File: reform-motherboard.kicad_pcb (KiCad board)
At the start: 4 copper layers, 130 x 99 mm, 208 parts, among them J1 TinyRex-J1-DF40C, J10 TEST_PMIC_ON, J11 TEST_ON, J12 USB_INT_3, J13 Conn_HDMI, J14 Conn_LVDS, J15 USB_INT_2, J16 Conn_LineIn, J17 Conn_LineOut, J18 TRRS, J19 Conn_BOOT, J2 TinyRex-J2-DF40C, J20 Conn_GPIO1, J21 Conn_01x06, J22 Conn_PWRON, J23 Conn_RESET, J24 Conn_01x04, J25 Conn_CONSOLE, J26 Conn_Backlight, J27 48099-5701, J3 TinyRex-J3-DF40C, J4 693072010801, J5 USB_A, J6 Barrel_Jack, J7 USB_A, J8 TEST_3V, J9 USB_INT_1, P1 5622-4100-ML, P2 J0G-0003NL, Q1 2N7002, Q3 2N7002, Q4 Si5481DU, SW1 SW_DIP_x01, U1 MPCIE-Socket, U10 SGTL5000XNAA3, U11 LP3962EMP-2.5, U12 SN74LVC1G08DCKR, U13 TLV1117-15, U14 CM2020-00TR, U15 TPS2044BDR, U16 TUSB2046BVFR, U2 LTC4156IUFDPBF, U3 TPS61235RWLR, U4 AP1501A-33K5G-13, U5 74AHC1G14, U6 INA260AIPW, U7 LTC4415IMSEPBF, U8 INA260AIPW, Y1 6MHz

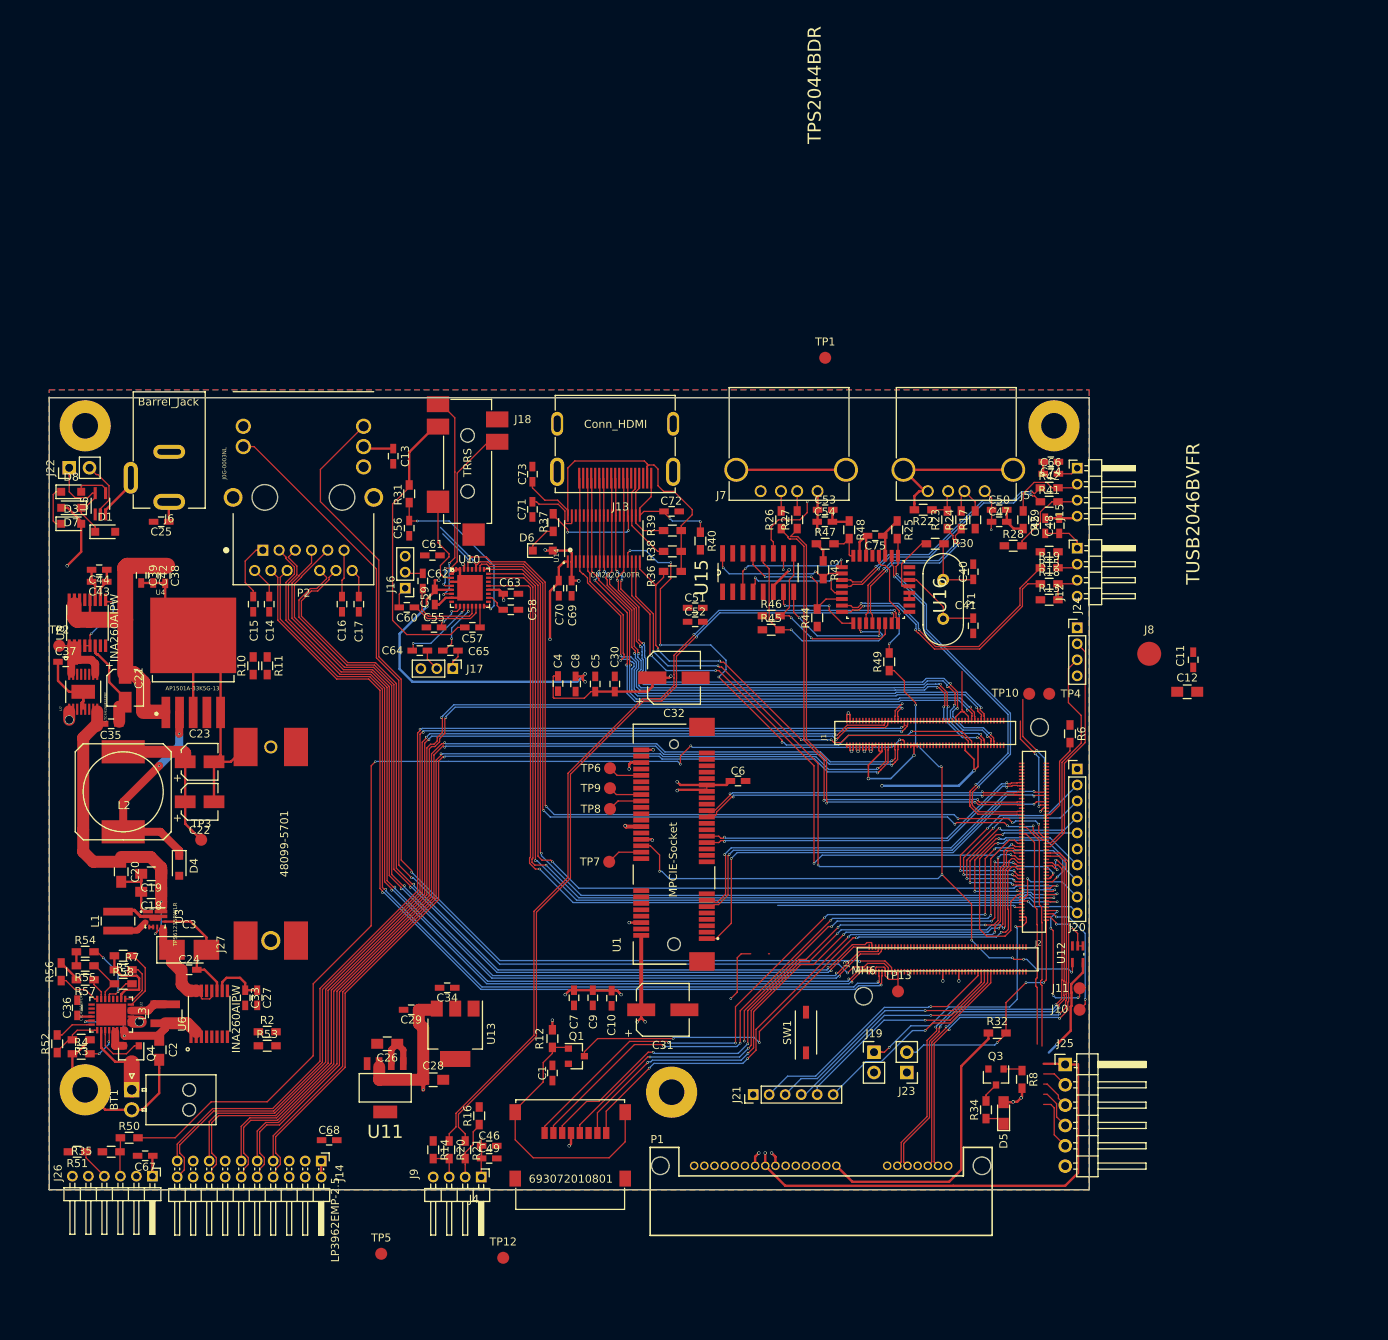
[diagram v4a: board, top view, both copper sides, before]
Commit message: Reform 0.2 main PCB routing WIP, 119 nets to go
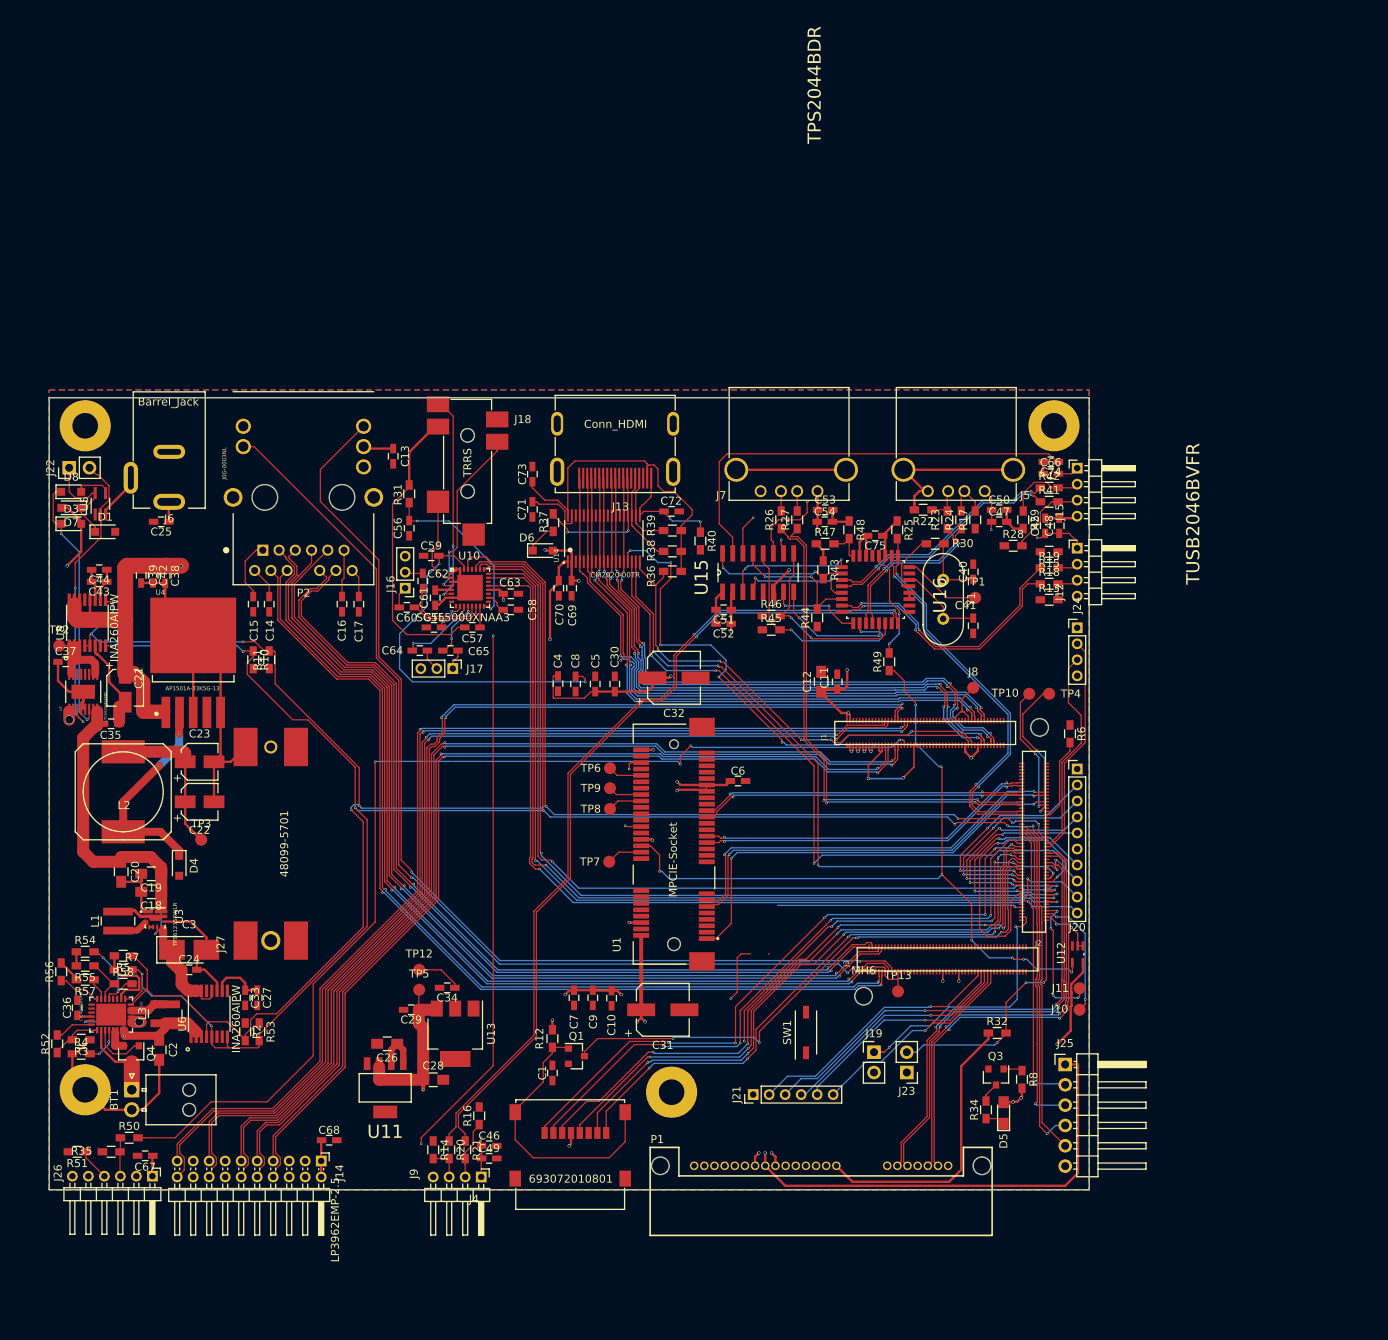
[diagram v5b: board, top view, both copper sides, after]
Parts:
- J8: footprint Measurement_Points:Measurement_Point_Round-SMD-Pad_Big -> Measurement_Points:Measurement_Point_Round-SMD-Pad_Small
- moved C12 45.8 mm to (126.5, 56.5), turned to 90 degrees
- moved C11 44.6 mm to (128.5, 56.5)
- moved TP12 37.5 mm to (76.2, 92.5)
- moved TP1 35.4 mm to (145.8, 46.0)
- moved TP5 33.3 mm to (76.2, 95.0)
- moved J8 22.4 mm to (145.5, 57.2)
- moved C61 5.31 mm to (78.2, 46.0), turned to 90 degrees
- moved C59 5.17 mm to (77.8, 40.8), turned to 0 degrees
- moved C51 3.56 mm to (114.3, 47.5), turned to 180 degrees
- moved C52 3.56 mm to (114.3, 49.2), turned to 180 degrees
- moved R2 2.75 mm to (54.5, 100.2), turned to 270 degrees
- moved R53 2.02 mm to (56.2, 100.2), turned to 270 degrees
- moved R11 0.79 mm to (57.5, 53.8), turned to 90 degrees
- moved R10 0.75 mm to (55.5, 53.8), turned to 270 degrees
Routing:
- net I2C3_SCL: track 125.9 -> 248.6 mm, vias 7 -> 9
- net I2C3_SDA: track 116.8 -> 237.1 mm, vias 5 -> 9
- net +5V: track 159.7 -> 278.7 mm, vias 13 -> 16
- net USB_HUB0_5V: track 4.14 -> 59.5 mm
- net USB_HUB1_5V: track 5.25 -> 48.0 mm, vias 0 -> 2
- net UART1_RTS: track 5.28 -> 42.4 mm, vias 0 -> 1
- net UART1_TXD: track 3.26 -> 35.8 mm, vias 0 -> 1
- net PWRON: track 7.40 -> 37.0 mm, vias 0 -> 2
- net POK_1V5: track 56.0 -> 85.3 mm, vias 10 -> 7
- net BATOFF: track 5.59 -> 32.9 mm, vias 0 -> 2
- net USB_HUB3_5V: track 104.4 -> 125.3 mm, vias 2 -> 4
- net Net-(TP1-Pad1): track 0.00 -> 9.81 mm
- net UART1_RXD: track 31.6 -> 38.9 mm, vias 0 -> 1
- net UART1_CTS: track 35.7 -> 42.5 mm
- net GND: track 196.8 -> 201.1 mm
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- removed copper zone on Power.Cu, net +1V5

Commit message: reform 0.2 main pcb done / rc1
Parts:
- removed Q3: 2N7002, TO_SOT_Packages_SMD:SOT-23
- removed SW1: SW_DIP_x01, Buttons_Switches_SMD:SW_DIP_x1_W5.08mm_Slide_Copal_CHS-A
- added G***: LOGO, mnt:mnt, F.Cu at (65.8, 56.6)
- added G***: LOGO, mnt:reform02, F.Cu at (80.1, 58.7)
- added J28: Conn_SDWP, Pin_Headers:Pin_Header_Straight_1x02_Pitch2.54mm, F.Cu at (124.0, 101.5)
- added J29: Conn_5V, Pin_Headers:Pin_Header_Angled_1x02_Pitch2.54mm, F.Cu at (153.2, 117.0)
- J22: footprint Pin_Headers:Pin_Header_Straight_1x02_Pitch2.54mm -> Pin_Headers:Pin_Header_Straight_1x02_Pitch2.00mm
- J24: footprint Pin_Headers:Pin_Header_Straight_1x04_Pitch2.00mm -> Pin_Headers:Pin_Header_Angled_1x04_Pitch2.00mm
- U2: footprint LTC4156IUFDPBF:QFN-28_UFD -> LTC4156-Custom:QFN-28_UFD
- moved R8 64.2 mm to (88.0, 97.8)
- moved BT1 32.4 mm to (72.5, 111.0), turned to 180 degrees
- moved C26 5.52 mm to (71.8, 96.2)
- moved U11 5.52 mm to (71.5, 101.8)
- moved D5 4.04 mm to (146.2, 107.8)
- moved TP5 2.92 mm to (74.8, 92.5)
- moved R34 1.55 mm to (147.5, 111.5), turned to 0 degrees
- moved C29 1.41 mm to (76.2, 96.5), turned to 90 degrees
- moved TP12 1.00 mm to (77.2, 92.5)
- moved J18 0.46 mm to (82.2, 29.6)
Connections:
- C37 pad 1: POK_5V -> Net-(C37-Pad1)
- J2 pad 34: GND -> Net-(J2-Pad34)
- J2 pad 7: POK_5V -> +5V
- R34 pad 2: Net-(Q3-Pad3) -> GND
- TP2 pad 1: POK_5V -> Net-(C37-Pad1)
- U7 pad 10: POK_5V -> Net-(C37-Pad1)
- U7 pad 15: POK_5V -> Net-(C37-Pad1)
- U7 pad 16: POK_5V -> Net-(C37-Pad1)
- U7 pad 9: POK_5V -> Net-(C37-Pad1)
- U8 pad 1: POK_5V -> Net-(C37-Pad1)
- U8 pad 2: POK_5V -> Net-(C37-Pad1)
- U8 pad 3: POK_5V -> Net-(C37-Pad1)
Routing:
- net GND: track 201.1 -> 352.6 mm, vias 0 -> 83
- net +5V: track 278.7 -> 426.5 mm, vias 16 -> 15
- net +3V3: track 192.0 -> 241.3 mm, vias 17 -> 33
- net POK_3V3: track 33.1 -> 75.4 mm, vias 1 -> 2
- net POK_1V5: track 85.3 -> 122.0 mm
- net Net-(BT1-Pad1): track 10.2 -> 43.5 mm, vias 0 -> 1
- net Net-(C18-Pad1): track 39.7 -> 68.0 mm, vias 2 -> 6
- net Net-(C37-Pad1): track 0.00 -> 16.5 mm
- net POK_5V: track 11.1 -> 0.00 mm
- net Net-(C24-Pad1): track 19.2 -> 29.0 mm
- net Net-(C25-Pad1): track 99.0 -> 105.9 mm, vias 3 -> 4
- net SD3_WP: track 50.5 -> 55.8 mm
- net POK_2V5: track 103.6 -> 107.9 mm
- net I2C3_SCL: track 248.6 -> 252.7 mm
- net Net-(Q3-Pad3): track 2.52 -> 0.00 mm
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- added copper zone on Power.Cu, net +3V3

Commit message: reform 0.2 main pcb sent to manufacture
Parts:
- moved TP12 0.79 mm to (77.0, 93.2)
- moved TP5 0.75 mm to (74.8, 93.2)

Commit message: motherboard 0.3 WIP snapshot schematics/PCB
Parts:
- removed BT1: Molex 105313-1202, Connectors_Molex:Molex_NanoFit_1x02x2.50mm_Angled
- removed G***: LOGO, mnt:mnt
- removed G***: LOGO, mnt:reform02
- removed P1: 5622-4100-ML, 5622-4100-ML:3M_5622-4100-ML
- removed Q4: Si5481DU, TO_SOT_Packages_SMD:SOT-23
- removed R41, R42: 27, Resistors_SMD:R_0603_HandSoldering
- removed R47, R48, R56, R58: 0, Resistors_SMD:R_0603_HandSoldering
- removed R50, R51: R0, Resistors_SMD:R_0603_HandSoldering
- removed R52: 100k, Resistors_SMD:R_0603_HandSoldering
- removed R53: 4.7k, Resistors_SMD:R_0603_HandSoldering
- removed R54, R55: 1.21k, Resistors_SMD:R_0603_HandSoldering
- removed R57: 3.6k, Resistors_SMD:R_0603_HandSoldering
- removed U16: TUSB2046BVFR, TUSB2046BVFR:QFP80P900X900X145-32N
- added C76: 10uF, Capacitors_SMD:C_0603_HandSoldering, F.Cu at (99.5, 104.0)
- added C77: 0.1uF, Capacitors_SMD:C_0603_HandSoldering, F.Cu at (99.5, 102.5)
- added C78: 33pF, Capacitors_SMD:C_0603_HandSoldering, F.Cu at (94.0, 102.5)
- added C79: 33pF, Capacitors_SMD:C_0603_HandSoldering, F.Cu at (96.0, 102.5)
- added C80: 33pF, Capacitors_SMD:C_0603_HandSoldering, F.Cu at (92.0, 102.5)
- added C81: 0.1uF, Capacitors_SMD:C_0603_HandSoldering, F.Cu at (104.0, 111.0)
- added C82: 10uF, Capacitors_SMD:C_0603_HandSoldering, F.Cu at (102.5, 99.0)
- added C83: 0.1uF, Capacitors_SMD:C_0603_HandSoldering, F.Cu at (137.5, 38.5)
- added C84: 0.1uF, Capacitors_SMD:C_0603_HandSoldering, F.Cu at (134.5, 57.0)
- added C85: 10uF, Capacitors_SMD:C_0603_HandSoldering, F.Cu at (137.5, 57.0)
- added C86: 0.1uF, Capacitors_SMD:C_0603_HandSoldering, F.Cu at (132.5, 38.5)
- added C87: 0.1uF, Capacitors_SMD:C_0603_HandSoldering, F.Cu at (143.5, 41.5)
- added C88: 0.1uF, Capacitors_SMD:C_0603_HandSoldering, F.Cu at (79.0, 116.0)
- added C89: 10uF, Capacitors_SMD:C_0603_HandSoldering, F.Cu at (75.0, 116.0)
- added C90: 0.1uF, Capacitors_SMD:C_0603_HandSoldering, F.Cu at (71.1, 116.0)
- added C91: 0.1uF, Capacitors_SMD:C_0603_HandSoldering, F.Cu at (75.0, 114.0)
- added D10: LED_WWAN, LEDs:LED_0805_HandSoldering, F.Cu at (103.5, 116.5)
- added D11: LED_3V3, LEDs:LED_0805_HandSoldering, F.Cu at (51.0, 24.2)
- added D2: PDS1040, PDS1040:DIO_SBR10U200P5-13, F.Cu at (51.0, 87.0)
- added D9: LED_WLAN, LEDs:LED_0805_HandSoldering, F.Cu at (103.4, 83.0)
- added J30: 48099-5701, 48099-5701:MOLEX_48099-5701, F.Cu at (176.8, 26.7)
- added J31: 48099-5701, 48099-5701:MOLEX_48099-5701, F.Cu at (60.3, 99.3)
- added J32: SIM_Card, TE-2199337-5:TE_2199337-5, F.Cu at (92.7, 112.7)
- added J33: BAT, Pin_Headers:Pin_Header_Angled_1x04_Pitch2.54mm, F.Cu at (43.5, 118.0)
- added L4: 220@100MHz, Choke_SMD:Choke_SMD_1206_Handsoldering, F.Cu at (149.5, 42.0)
- added L5: 220@100MHz, Choke_SMD:Choke_SMD_1206_Handsoldering, F.Cu at (149.5, 44.0)
- added Q2: Si2333DDS, TO_SOT_Packages_SMD:SOT-23, F.Cu at (40.8, 83.2)
- added Q3: Si7288DP, Housings_SOIC:PowerPAK_SO-8_Dual, F.Cu at (51.9, 93.9)
- added Q5: Si2333DDS, TO_SOT_Packages_SMD:SOT-23, F.Cu at (37.0, 83.2)
- added R1: 100k, Resistors_SMD:R_0603_HandSoldering, F.Cu at (53.4, 97.7)
- added R33: 4.7k, Resistors_SMD:R_0603_HandSoldering, F.Cu at (127.5, 50.0)
- added R9: 330, Resistors_SMD:R_0603_HandSoldering, F.Cu at (34.0, 113.5)
- added TP11: WWAN_UART_TX, Measurement_Points:Measurement_Point_Round-SMD-Pad_Small, F.Cu at (117.0, 125.0)
- added TP14: WWAN_UART_RX, Measurement_Points:Measurement_Point_Round-SMD-Pad_Small, F.Cu at (115.0, 126.0)
- added TP15: TEST_5V, Measurement_Points:Measurement_Point_Round-SMD-Pad_Small, F.Cu at (27.8, 76.0)
- added TP16: WWAN_WAKE_OUT, Measurement_Points:Measurement_Point_Round-SMD-Pad_Small, F.Cu at (115.0, 130.0)
- added TP17: WWAN_RFKILL, Measurement_Points:Measurement_Point_Round-SMD-Pad_Small, F.Cu at (108.0, 129.0)
- added U9: TUSB4041IPAPR, TUSB4041IPAPR:QFP50P1200X1200X105-65N, F.Cu at (135.8, 47.9)
- C2: value 22uF -> 1uF; footprint Capacitors_SMD:C_0805_HandSoldering -> Capacitors_SMD:C_0603_HandSoldering
- C25, C66: value 10uF -> 0.1uF
- C35, C37: value 4.7uF -> 0.1uF
- C36: value 0.047uF -> 0.1uF
- C40, C41: value 27pF -> 18pF
- C42: value 0.1uF -> 100uF; footprint Capacitors_SMD:C_0603_HandSoldering -> Capacitors_SMD:C_0805_HandSoldering
- C43: value 10uF -> 1uF
- C44: value 0.1uF -> 1uF
- C45, C46, C47, C53: value 10uF -> 22uF
- C74: value 0.1uF -> 10uF
- D1: value D_Schottky -> D_Zener
- D3: value D -> LED_CStat2; footprint Diodes_SMD:D_SOD-323_HandSoldering -> LEDs:LED_0805_HandSoldering
- D5: value LED_3V3 -> ZLLS350; footprint LEDs:LED_0805_HandSoldering -> Diodes_SMD:D_SOD-523
- D7: value D_Schottky -> LED_Charge; footprint Diodes_SMD:D_SOD-323_HandSoldering -> LEDs:LED_0805_HandSoldering
- D8: value D -> PDS1040; footprint Diodes_SMD:D_SOD-323_HandSoldering -> PDS1040:DIO_SBR10U200P5-13
- J15: value USB_INT_2 -> Conn_01x03; footprint Pin_Headers:Pin_Header_Angled_1x04_Pitch2.00mm -> Pin_Headers:Pin_Header_Straight_1x03_Pitch2.54mm
- J22: value Conn_PWRON -> Conn_01x02; footprint Pin_Headers:Pin_Header_Straight_1x02_Pitch2.00mm -> Pin_Headers:Pin_Header_Straight_1x02_Pitch2.54mm
- L3: value 1 uH -> 10 uH
- R11: value 4.7k -> 240
- R13, R14, R15, R16: value 15k -> 0
- R17, R29: value 15k -> 240
- R2: value 4.7k -> 100k
- R22: value 15k -> 9.53k
- R25: value 1.5k -> 10k
- R28: value 15k -> 90.9k
- R3: value 100k -> 0
- R30: value 1.5k -> 1M
- R34: value 240 -> 4.7k
- R35: value R0 -> 4.7k
- R4: value 499 -> 0
- R5: value 4.7k -> 20m; footprint Resistors_SMD:R_0603_HandSoldering -> Resistors_SMD:R_1206_HandSoldering
- R7: value 4.7k -> 330
- R8: value 0 -> 3.6k
- TP1: value TEST_USB_SUSP -> SATA_DA
- TP2: value TEST_5V -> TEST_BATOUT
- TP6: value PCIe_WLANn -> TEST_1V1
- TP8: value PCIe_USB_D- -> UIM_C4
- TP9: value PCIe_USB_D+ -> UIM_C8
- U2: value LTC4156IUFDPBF -> BQ24650RVAT; footprint LTC4156-Custom:QFN-28_UFD -> BQ24650RVAT:QFN50P350X350X100-17N
- U5: value 74AHC1G14 -> TLV74311PDBVR; footprint TO_SOT_Packages_SMD:SOT-353_SC-70-5_Handsoldering -> TO_SOT_Packages_SMD:SOT-223
- U7: value LTC4415IMSEPBF -> MPCIE-Socket; footprint LTC4415IMSEPBF:MSOP-16_MSE -> 67910-5700:MOLEX_67910-5700
- U8: value INA260AIPW -> MPCIE-Socket; footprint INA260AIPW:SOP65P640X120-16N -> 67910-5700:MOLEX_67910-5700
- Y1: value 6MHz -> 24MHz; footprint Crystals:Crystal_HC49-4H_Vertical -> Crystals:Crystal_SMD_5032-2pin_5.0x3.2mm_HandSoldering
- moved U7 142.0 mm to (174.9, 77.1), turned to 0 degrees
- moved U5 121.6 mm to (157.0, 49.5), turned to 0 degrees
- moved C43 115.6 mm to (151.5, 52.5), turned to 270 degrees
- moved C44 115.4 mm to (151.5, 48.0), turned to 90 degrees
- moved R35 113.5 mm to (127.5, 45.7), turned to 270 degrees
- moved D5 106.7 mm to (39.7, 102.9), turned to 180 degrees
- moved C46 105.4 mm to (190.3, 114.9)
- moved C49 105.4 mm to (190.3, 116.5)
- moved J9 105.4 mm to (189.3, 118.8)
- moved R20 105.4 mm to (185.3, 115.4)
- moved R21 105.4 mm to (187.3, 115.4)
- moved R29 101.2 mm to (50.8, 29.2)
- moved U8 92.0 mm to (110.7, 101.2)
- moved R17 88.7 mm to (107.0, 116.0), turned to 180 degrees
- moved TP2 85.7 mm to (48.0, 136.0)
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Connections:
- net Net-(J2-Pad10) renamed GPIO3
- C2 pad 1: Net-(C2-Pad1) -> CHGVCC
- C25 pad 2: GND -> Net-(C25-Pad2)
- C27 pad 1: +3V3 -> Net-(C27-Pad1)
- C33 pad 1: +3V3 -> Net-(C27-Pad1)
- C35 pad 1: Net-(C18-Pad1) -> Net-(C35-Pad1)
- C35 pad 2: GND -> Net-(C24-Pad1)
- C36 pad 1: Net-(C36-Pad1) -> Net-(C35-Pad1)
- C37 pad 1: Net-(C37-Pad1) -> Net-(C24-Pad1)
- C38 pad 1: +5V -> Net-(C24-Pad1)
- C39 pad 1: +5V -> Net-(C39-Pad1)
- C42 pad 1: +5V -> Net-(C42-Pad1)
- C43 pad 1: +3V3 -> POK_1V5
- C44 pad 1: +3V3 -> +1V1
- C66 pad 1: USB_HUB0_5V -> +3V3
- C67 pad 1: +5V -> GND
- C67 pad 2: GND -> +5V
- C68 pad 1: +3V3 -> GND
- C68 pad 2: GND -> +3V3
- C74 pad 1: USB_HUB0_5V -> +3V3
- C75 pad 1: +3V3 -> Net-(C75-Pad1)
- D1 pad 1: Net-(D1-Pad1) -> CHGVCC
- D1 pad 2: Net-(C18-Pad1) -> GND
- D3 pad 1: BATOFF -> Net-(D3-Pad1)
- D3 pad 2: Net-(C25-Pad1) -> Net-(D3-Pad2)
- D5 pad 1: Net-(D5-Pad1) -> Net-(C25-Pad1)
- D5 pad 2: +3V3 -> Net-(C39-Pad1)
- D7 pad 1: Net-(D1-Pad1) -> Net-(D7-Pad1)
- D7 pad 2: Net-(C25-Pad1) -> Net-(D7-Pad2)
- D8 pad 1: BATOFF -> Net-(C42-Pad1)
- D8 pad 2: Net-(D8-Pad2) -> CHGVCC
- J1 pad 38: LVDS0_PWM -> GPIO2
- J14 pad 4: Net-(J14-Pad4) -> +3V3
- J15 pad 1: USB_HUB0_5V -> +5V
- J15 pad 2: Net-(J15-Pad2) -> FAN_PWM
- J15 pad 3: Net-(J15-Pad3) -> GND
- J2 pad 17: Net-(J2-Pad17) -> LVDS0_PWM
- J2 pad 19: Net-(J2-Pad19) -> FAN_PWM
- J2 pad 66: Net-(J2-Pad66) -> GND
- J2 pad 68: Net-(J2-Pad66) -> Net-(J2-Pad68)
- J2 pad 7: +5V -> POK_5V
- J20 pad 7: Net-(J2-Pad19) -> Net-(J20-Pad7)
- J20 pad 8: Net-(J2-Pad17) -> Net-(J20-Pad8)
- J22 pad 1: Net-(D1-Pad1) -> +5V
- J22 pad 2: PWRON -> Net-(C42-Pad1)
- J26 pad 3: Net-(J26-Pad3) -> +3V3
- J26 pad 4: Net-(J26-Pad4) -> LVDS0_PWM
- J6 pad 1: Net-(C25-Pad1) -> CHGVCC
- L3 pad 1: Net-(C2-Pad1) -> Net-(C25-Pad2)
- L3 pad 2: Net-(L3-Pad2) -> Net-(C35-Pad1)
- R10 pad 1: I2C3_SDA -> GND
- R10 pad 2: +3V3 -> Net-(C24-Pad1)
- R11 pad 2: I2C3_SCL -> Net-(D9-Pad2)
- R13 pad 1: GND -> Net-(C76-Pad2)
- R13 pad 2: Net-(J12-Pad3) -> UIM_PWR
- R14 pad 2: Net-(J9-Pad3) -> UIM_DET
- R15 pad 1: Net-(J12-Pad2) -> Net-(J32-Pad6)
- R15 pad 2: GND -> UIM_VPP
- R16 pad 1: Net-(J9-Pad2) -> RESETn
- R16 pad 2: GND -> Net-(R16-Pad2)
- R17 pad 1: GND -> +3V3
- R17 pad 2: Net-(J5-Pad2) -> Net-(D10-Pad2)
- R2 pad 1: +3V3 -> Net-(R2-Pad1)
- R2 pad 2: I2C3_SCL -> GND
- R22 pad 1: Net-(J5-Pad3) -> GND
- R22 pad 2: GND -> Net-(R22-Pad2)
- R25 pad 1: +3V3 -> GND
- R25 pad 2: USB1_P -> Net-(R25-Pad2)
- R28 pad 1: GND -> +5V
- R28 pad 2: Net-(J15-Pad3) -> Net-(R25-Pad2)
- R29 pad 1: Net-(J15-Pad2) -> Net-(D11-Pad1)
- R3 pad 1: GND -> Net-(R3-Pad1)
- R30 pad 1: Net-(R30-Pad1) -> Net-(C40-Pad1)
- R30 pad 2: Net-(C40-Pad1) -> Net-(C41-Pad1)
- R34 pad 1: Net-(D5-Pad1) -> Net-(R34-Pad1)
- R35 pad 1: Net-(J26-Pad3) -> Net-(R35-Pad1)
- R35 pad 2: +3V3 -> GND
- R4 pad 1: GND -> Net-(R4-Pad1)
- R4 pad 2: Net-(R4-Pad2) -> Net-(R3-Pad2)
- R49 pad 1: RESETn -> Net-(R49-Pad1)
- R49 pad 2: Net-(R49-Pad2) -> RESETn
- R5 pad 1: I2C3_SCL -> Net-(C35-Pad1)
- R5 pad 2: +3V3 -> Net-(C24-Pad1)
- R6 pad 2: Net-(J2-Pad66) -> Net-(J2-Pad68)
- R7 pad 1: +3V3 -> CHGVCC
- R7 pad 2: I2C3_SDA -> Net-(D3-Pad2)
- R8 pad 1: POK_3V3 -> Net-(C24-Pad1)
- R8 pad 2: +3V3 -> Net-(R8-Pad2)
- TP2 pad 1: Net-(C37-Pad1) -> Net-(C24-Pad1)
- TP6 pad 1: Net-(TP6-Pad1) -> +1V1
- U1 pad 36: Net-(TP8-Pad1) -> Net-(U1-Pad36)
- U1 pad 38: Net-(TP9-Pad1) -> Net-(U1-Pad38)
- U1 pad 44: Net-(TP6-Pad1) -> Net-(D9-Pad1)
- U11 pad 1: +3V3 -> PWRON
- U2 pad 1: I2C3_SDA -> CHGVCC
- U2 pad 10: Net-(U2-Pad10) -> Net-(C35-Pad1)
- U2 pad 11: Net-(U2-Pad11) -> GND
- U2 pad 12: Net-(C36-Pad1) -> Net-(C39-Pad1)
- U2 pad 13: Net-(C2-Pad1) -> Net-(Q3-Pad4)
- U2 pad 14: Net-(R52-Pad2) -> Net-(C25-Pad2)
- U2 pad 15: Net-(R3-Pad2) -> Net-(Q3-Pad2)
- U2 pad 16: Net-(BT1-Pad1) -> Net-(C25-Pad1)
- U2 pad 17: Net-(Q4-Pad1) -> GND
- U2 pad 2: +3V3 -> Net-(R4-Pad1)
- U2 pad 3: Net-(U2-Pad3) -> Net-(D7-Pad1)
- U2 pad 4: Net-(U2-Pad4) -> Net-(R2-Pad1)
- U2 pad 5: Net-(R54-Pad2) -> Net-(D3-Pad1)
- U2 pad 6: Net-(R55-Pad1) -> Net-(R3-Pad2)
- U2 pad 7: Net-(R57-Pad1) -> Net-(R3-Pad1)
- U2 pad 8: Net-(R56-Pad1) -> Net-(R8-Pad2)
- U2 pad 9: Net-(U2-Pad9) -> Net-(C24-Pad1)
- U3 pad 7: Net-(C24-Pad1) -> PWRON
- U5 pad 1: (no net) -> GND
- U5 pad 2: PWRON -> +1V1
- U5 pad 3: GND -> POK_1V5
- U5 pad 4: Net-(D8-Pad2) -> (no net)
- U6 pad 1: Net-(C2-Pad1) -> BATVCC
- U6 pad 10: +3V3 -> Net-(C27-Pad1)
- U6 pad 12: Net-(C24-Pad1) -> BATVCC
- U6 pad 2: Net-(C2-Pad1) -> BATVCC
- U6 pad 3: Net-(C2-Pad1) -> BATVCC
- U7 pad 1: Net-(C25-Pad1) -> Net-(U7-Pad1)
- U7 pad 10: Net-(C37-Pad1) -> Net-(U7-Pad10)
- U7 pad 15: Net-(C37-Pad1) -> GND
- U7 pad 16: Net-(C37-Pad1) -> Net-(U7-Pad16)
- U7 pad 17: GND -> Net-(U7-Pad17)
- U7 pad 2: Net-(C25-Pad1) -> +3V3
- U7 pad 3: PWRON -> Net-(U7-Pad3)
- U7 pad 4: GND -> Net-(U7-Pad4)
- U7 pad 5: GND -> Net-(U7-Pad5)
- U7 pad 6: BATOFF -> Net-(U7-Pad6)
- U7 pad 7: Net-(C18-Pad1) -> Net-(U7-Pad7)
- U7 pad 8: Net-(C18-Pad1) -> Net-(U7-Pad8)
- U7 pad 9: Net-(C37-Pad1) -> Net-(U7-Pad9)
- U8 pad 1: Net-(C37-Pad1) -> Net-(TP16-Pad1)
- U8 pad 10: +3V3 -> UIM_DATA
- U8 pad 11: GND -> Net-(TP14-Pad1)
- U8 pad 12: +5V -> UIM_CLK
- U8 pad 14: +5V -> UIM_RST
- U8 pad 15: +5V -> GND
- U8 pad 16: +5V -> UIM_VPP
- U8 pad 2: Net-(C37-Pad1) -> +3V3
- U8 pad 3: Net-(C37-Pad1) -> Net-(U8-Pad3)
- U8 pad 4: I2C3_SCL -> GND
- U8 pad 5: I2C3_SCL -> Net-(U8-Pad5)
- U8 pad 6: GND -> POK_1V5
- U8 pad 8: I2C3_SDA -> UIM_PWR
- U8 pad 9: I2C3_SCL -> GND
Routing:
- net +5V: track 426.8 -> 112.8 mm, vias 15 -> 12
- net I2C3_SDA: track 237.6 -> 3.88 mm, vias 9 -> 0
- net +3V3: track 241.3 -> 51.8 mm, vias 33 -> 6
- net GND: track 352.6 -> 169.7 mm, vias 83 -> 43
- net I2C3_SCL: track 252.7 -> 112.0 mm, vias 9 -> 4
- net LVDS0_PWM: track 135.0 -> 0.00 mm, vias 4 -> 0
- net POK_1V5: track 121.6 -> 6.94 mm, vias 7 -> 0
- net Net-(C25-Pad1): track 105.9 -> 6.48 mm, vias 4 -> 2
- net RESETn: track 94.6 -> 0.00 mm, vias 8 -> 0
- net USB_HUB1_P: track 32.5 -> 117.6 mm
- net USB_HUB1_N: track 33.2 -> 117.5 mm
- net SD3_DATA3: track 81.1 -> 0.00 mm, vias 4 -> 0
- net SD3_CMD: track 79.8 -> 0.00 mm, vias 6 -> 0
- net USB_HUB3_5V: track 125.3 -> 46.9 mm, vias 4 -> 2
- net POK_2V5: track 107.7 -> 29.7 mm, vias 3 -> 2
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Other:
- board size 130 x 99 mm -> 163 x 99 mm
- net class PWRFAT added: clearance 0.15, trace_width 0.5, via_dia 0.6, via_drill 0.5
